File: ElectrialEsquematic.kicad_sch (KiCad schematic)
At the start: 12 parts, among them U2 ESP32_NODEMCU, U3 TP4056

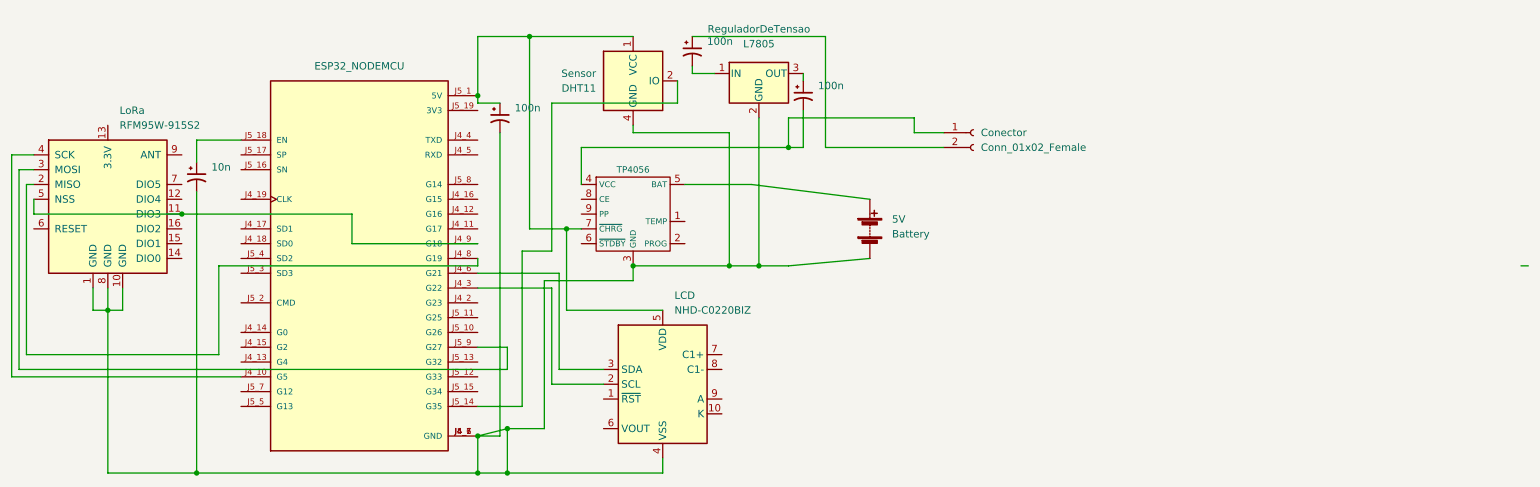
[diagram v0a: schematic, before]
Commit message: Add netlist
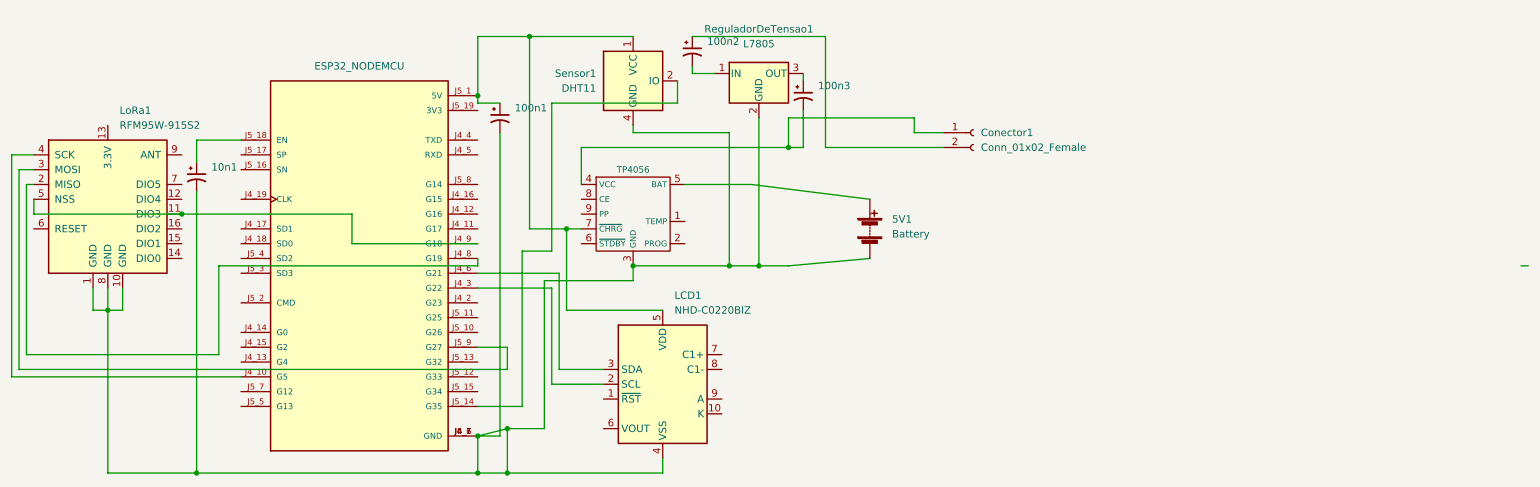
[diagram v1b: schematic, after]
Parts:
- renumbered 100n to 100n1, 100n to 100n2, 100n to 100n3, 10n to 10n1, 5V to 5V1, Conector to Conector1, LCD to LCD1, LoRa to LoRa1, ReguladorDeTensao to ReguladorDeTensao1, Sensor to Sensor1
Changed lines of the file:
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@@
   (symbol (lib_id "Sensor:DHT11") (at 151.13 58.42 0) (unit 1)
     (in_bom yes) (on_board yes) (fields_autoplaced)
-    (property "Reference" "Sensor" (id 0) (at 144.78 57.1499 0)
+    (property "Reference" "Sensor1" (id 0) (at 144.78 57.1499 0)
       (effects (font (size 1.27 1.27)) (justify right))
     )
@@
   (symbol (lib_id "Device:C_Polarized_Small_US") (at 161.29 53.34 0) (unit 1)
     (in_bom yes) (on_board yes) (fields_autoplaced)
-    (property "Reference" "100n" (id 0) (at 163.83 51.6381 0)
+    (property "Reference" "100n2" (id 0) (at 163.83 51.6381 0)
       (effects (font (size 1.27 1.27)) (justify left))
     )
@@
   (symbol (lib_id "RF_Module:RFM95W-915S2") (at 60.96 78.74 0) (unit 1)
     (in_bom yes) (on_board yes) (fields_autoplaced)
-    (property "Reference" "LoRa" (id 0) (at 62.9794 63.5 0)
+    (property "Reference" "LoRa1" (id 0) (at 62.9794 63.5 0)
       (effects (font (size 1.27 1.27)) (justify left))
     )
@@
   (symbol (lib_id "Connector:Conn_01x02_Female") (at 209.55 67.31 0) (unit 1)
     (in_bom yes) (on_board yes) (fields_autoplaced)
-    (property "Reference" "Conector" (id 0) (at 210.82 67.3099 0)
+    (property "Reference" "Conector1" (id 0) (at 210.82 67.3099 0)
       (effects (font (size 1.27 1.27)) (justify left))
     )
@@
   (symbol (lib_id "Device:C_Polarized_Small_US") (at 128.27 64.77 0) (unit 1)
     (in_bom yes) (on_board yes) (fields_autoplaced)
-    (property "Reference" "100n" (id 0) (at 130.81 63.0681 0)
+    (property "Reference" "100n1" (id 0) (at 130.81 63.0681 0)
       (effects (font (size 1.27 1.27)) (justify left))
     )
@@
   (symbol (lib_id "Display_Character:NHD-C0220BIZ") (at 156.21 110.49 0) (unit 1)
     (in_bom yes) (on_board yes) (fields_autoplaced)
-    (property "Reference" "LCD" (id 0) (at 158.2294 95.25 0)
+    (property "Reference" "LCD1" (id 0) (at 158.2294 95.25 0)
       (effects (font (size 1.27 1.27)) (justify left))
     )
@@
   (symbol (lib_id "Device:C_Polarized_Small_US") (at 180.34 60.96 0) (unit 1)
     (in_bom yes) (on_board yes) (fields_autoplaced)
-    (property "Reference" "100n" (id 0) (at 182.88 59.2581 0)
+    (property "Reference" "100n3" (id 0) (at 182.88 59.2581 0)
       (effects (font (size 1.27 1.27)) (justify left))
     )
@@
   (symbol (lib_id "Regulator_Linear:L7805") (at 172.72 57.15 0) (unit 1)
     (in_bom yes) (on_board yes) (fields_autoplaced)
-    (property "Reference" "ReguladorDeTensao" (id 0) (at 172.72 49.53 0))
+    (property "Reference" "ReguladorDeTensao1" (id 0) (at 172.72 49.53 0))
     (property "Value" "L7805" (id 1) (at 172.72 52.07 0))
     (property "Footprint" "" (id 2) (at 173.355 60.96 0)
@@
   (symbol (lib_id "Device:C_Polarized_Small_US") (at 76.2 74.93 0) (unit 1)
     (in_bom yes) (on_board yes) (fields_autoplaced)
-    (property "Reference" "10n" (id 0) (at 78.74 73.2281 0)
+    (property "Reference" "10n1" (id 0) (at 78.74 73.2281 0)
       (effects (font (size 1.27 1.27)) (justify left))
     )
@@
   (symbol (lib_id "Device:Battery") (at 191.77 83.82 0) (unit 1)
     (in_bom yes) (on_board yes) (fields_autoplaced)
-    (property "Reference" "5V" (id 0) (at 195.58 82.1689 0)
+    (property "Reference" "5V1" (id 0) (at 195.58 82.1689 0)
       (effects (font (size 1.27 1.27)) (justify left))
     )
@@
   (symbol_instances
     (path "/fe08bd02-0b12-48e4-8410-c20f79b2f692"
-      (reference "5V") (unit 1) (value "Battery") (footprint "")
+      (reference "5V1") (unit 1) (value "Battery") (footprint "")
     )
     (path "/fa57424c-1a87-42d8-8df8-ed5f102301f4"
-      (reference "10n") (unit 1) (value "Capacitor") (footprint "")
+      (reference "10n1") (unit 1) (value "Capacitor") (footprint "")
+    )
+    (path "/8c9c2f71-2b7f-4070-8d97-a1f034d62ec9"
+      (reference "100n1") (unit 1) (value "Capacitor") (footprint "")
     )
     (path "/5e279f2e-23c5-4795-a7c8-145ee445dd00"
-      (reference "100n") (unit 1) (value "Capacitor") (footprint "")
-    )
-    (path "/8c9c2f71-2b7f-4070-8d97-a1f034d62ec9"
-      (reference "100n") (unit 1) (value "Capacitor") (footprint "")
+      (reference "100n2") (unit 1) (value "Capacitor") (footprint "")
     )
     (path "/b769f63b-a3d3-44a7-94e5-34ca824e007d"
-      (reference "100n") (unit 1) (value "Capacitor") (footprint "")
+      (reference "100n3") (unit 1) (value "Capacitor") (footprint "")
     )
     (path "/8644b6a1-89d7-44d8-87ac-938fc6afa77b"
-      (reference "Conector") (unit 1) (value "Conn_01x02_Female") (footprint "")
+      (reference "Conector1") (unit 1) (value "Conn_01x02_Female") (footprint "")
     )
     (path "/a280483b-a52c-485b-ba39-1279f12be1a1"
-      (reference "LCD") (unit 1) (value "NHD-C0220BIZ") (footprint "Display:NHD-C0220BiZ")
+      (reference "LCD1") (unit 1) (value "NHD-C0220BIZ") (footprint "Display:NHD-C0220BiZ")
     )
     (path "/6307bb6d-2ec1-48a3-990f-c61c20fe671e"
-      (reference "LoRa") (unit 1) (value "RFM95W-915S2") (footprint "")
+      (reference "LoRa1") (unit 1) (value "RFM95W-915S2") (footprint "")
     )
     (path "/c39d33a7-d9f6-4010-866f-494adbad79da"
-      (reference "ReguladorDeTensao") (unit 1) (value "L7805") (footprint "")
+      (reference "ReguladorDeTensao1") (unit 1) (value "L7805") (footprint "")
     )
     (path "/0cab0ab6-e788-44e1-9870-0a49cd0b2dc7"
-      (reference "Sensor") (unit 1) (value "DHT11") (footprint "Sensor:Aosong_DHT11_5.5x12.0_P2.54mm")
+      (reference "Sensor1") (unit 1) (value "DHT11") (footprint "Sensor:Aosong_DHT11_5.5x12.0_P2.54mm")
     )
     (path "/6ec32f14-bbdc-4f0d-b679-c67f7cd3b0ce"

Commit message: Mudando o regulador de tensao, mais economico para o uso da bateria
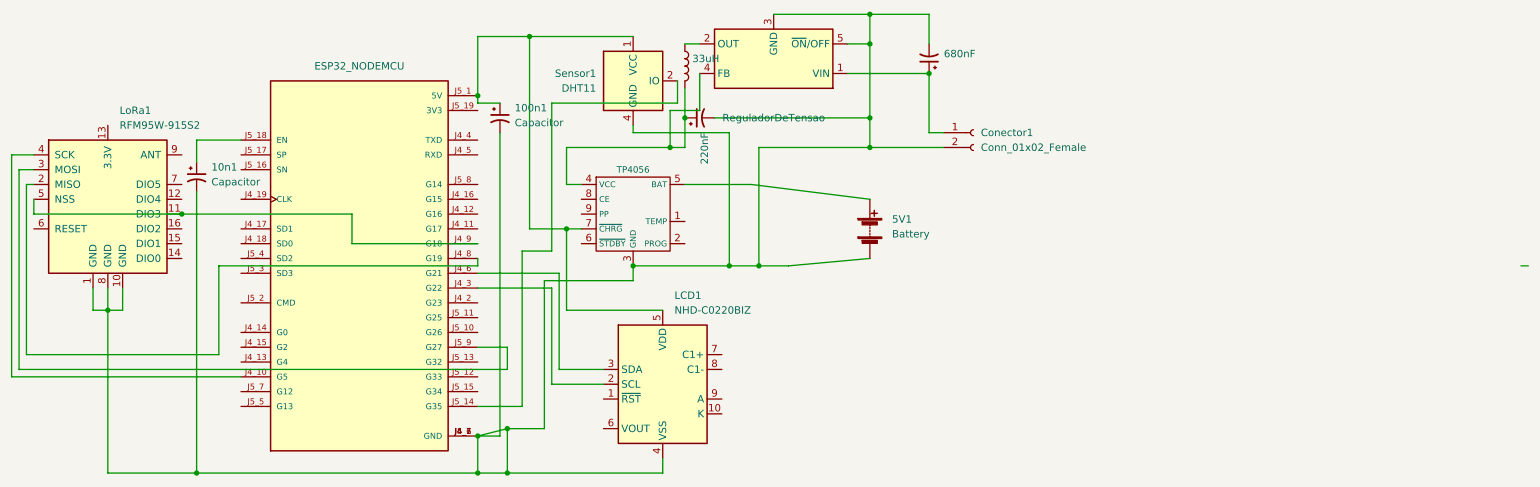
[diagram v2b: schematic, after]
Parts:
- removed ReguladorDeTensao1: L7805, symbol Regulator_Linear:L7805
- added 33uH: (no value), symbol Device:L
- added ReguladorDeTensao: (no value), symbol Regulator_Switching:LM2596S-5
- 100n1, 10n1: value (none) -> Capacitor
- renumbered 100n2 to 220nF, 100n3 to 680nF
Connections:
- net at 100n1.2, 10n1.2, 5V1.2 (-)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: now also 220nF.2, 680nF.2, Conector1.2 (Pin_2), ReguladorDeTensao.3 (GND), ReguladorDeTensao.5 (~{ON}/OFF)
- net at 220nF.1: now also U3.4 (VCC), 33uH.2, ReguladorDeTensao.4 (FB); no longer Conector1.2 (Pin_2)
- net at 680nF.1: now also Conector1.1 (Pin_1), ReguladorDeTensao.1 (VIN)
- new net: 33uH.1, ReguladorDeTensao.2 (OUT)
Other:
- moved on the sheet: 220nF, 680nF

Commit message: Atualizando o Sensor de temperatura e Umidade
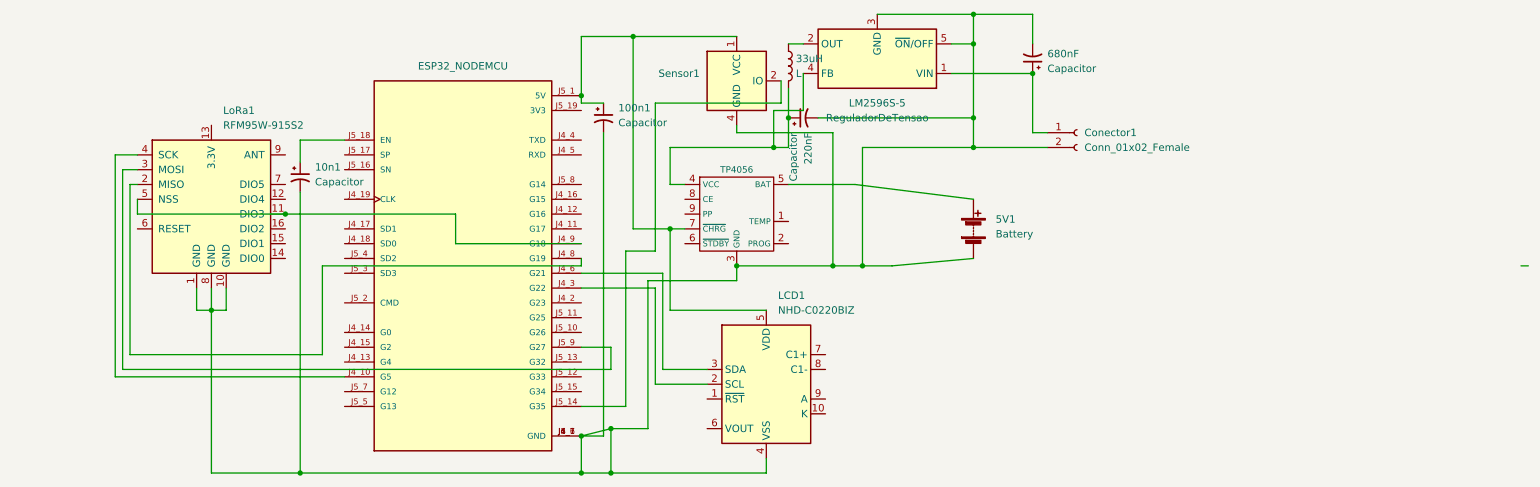
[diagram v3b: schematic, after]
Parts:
- 220nF, 680nF: value (none) -> Capacitor
- 33uH: value (none) -> L
- ReguladorDeTensao: value (none) -> LM2596S-5; footprint (none) -> Package_TO_SOT_SMD:TO-263-5_TabPin3
- Sensor1: value DHT11 -> (none); footprint Sensor:Aosong_DHT11_5.5x12.0_P2.54mm -> (none)
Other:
- moved on the sheet: 100n1, 10n1, 220nF, 33uH, 5V1, 680nF, Conector1, LCD1, LoRa1, ReguladorDeTensao, Sensor1
